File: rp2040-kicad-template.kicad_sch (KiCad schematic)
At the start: 48 parts, among them U1 RP2040, U2 TYPE-C-31-M-12, U3 XC6206PxxxMR, U4 PJ-320A, U5 USB Boot, U6 Reset, U7 W25Q16JVUXIQ, Y1 12MHz - 20pF

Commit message: Add parts libraries
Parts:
- removed D1: 5819W, Diode_SMD:D_SOD-123, symbol Device:D_Schottky_Small
- removed TP1: Debug 5V, TestPoint:TestPoint_Pad_D2.0mm, symbol Connector:TestPoint_Small
- removed U2: TYPE-C-31-M-12, footprints:simple-usb-c, symbol simple-usb-c:TYPE-C-31-M-12
- removed U4: PJ-320A, footprints:trrs-connector-pj320a, symbol trss-connector-pj320a:PJ-320A
- added U4: TYPE-C-31-M-12, footprint:USB-C_SMD-TYPE-C-31-M-12, symbol simple-usb-c:TYPE-C-31-M-12
- added U8: PJ-320A, footprint:AUDIO-TH_XKB_PJ-320A, symbol trrs-connector-pj320a:PJ-320A
- U3: footprint Package_TO_SOT_SMD:SOT-23 -> Package_TO_SOT_SMD:SOT-23-3
- U7: footprint footprints:w25q16jvuxiq -> footprint:USON-8_L3.0-W2.0-P0.50-BL-EP; LCSC Part # (none) -> C2843335
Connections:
- net CC1: now also U4.A5 (CC1)
- net CC2: now also U4.B5 (CC2)
- net GND: now also U4.A1 (GND), U4.A12 (GND), U4.B1 (GND), U4.B12 (GND), U8.5
- net SWCLK: now also U8.3
- net SWD: now also U8.4
- net USB+: now also U4.A6 (DP1), U4.B6 (DP2)
- net USB-: now also U4.A7 (DN1), U4.B7 (DN2)
- net VBUS: now also U4.A4 (VBUS), U4.A9 (VBUS), U4.B4 (VBUS), U4.B9 (VBUS)
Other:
- moved on the sheet: C11, C12, C13, C14, C15, C17, C18, C19, R7, R9, TP7, U3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

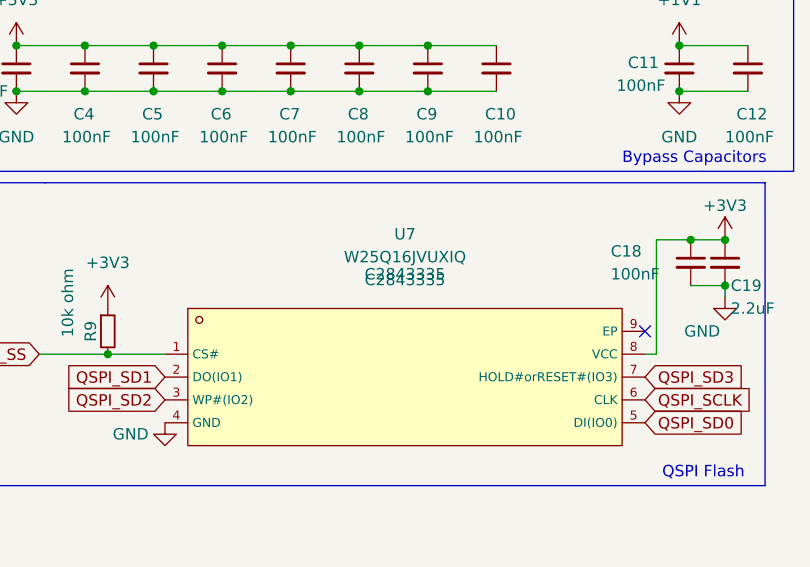
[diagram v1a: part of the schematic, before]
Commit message: Update some footprint references and use the newer footprint library
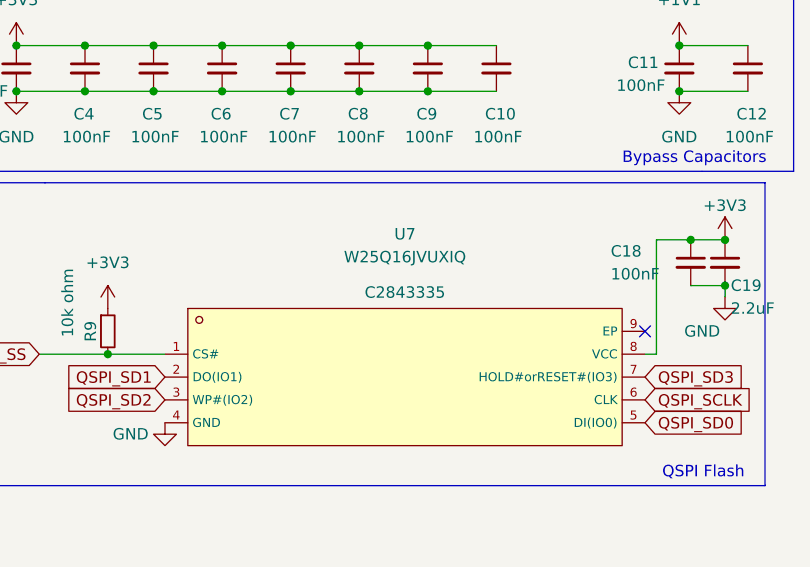
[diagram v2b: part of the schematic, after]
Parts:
- U4: footprint footprint:USB-C_SMD-TYPE-C-31-M-12 -> footprints:simple-usb-c
- U7: footprint footprint:USON-8_L3.0-W2.0-P0.50-BL-EP -> footprints:w25q16jvuxiq; LCSC Part # C2843335 -> (none)
- U8: footprint footprint:AUDIO-TH_XKB_PJ-320A -> footprints:trrs-connector-pj320a
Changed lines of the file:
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@@
 			)
 		)
-		(property "Footprint" "footprint:AUDIO-TH_XKB_PJ-320A"
+		(property "Footprint" "footprints:trrs-connector-pj320a"
 			(at 73.66 55.88 0)
 			(effects
@@
 		(on_board yes)
 		(dnp no)
-		(fields_autoplaced yes)
 		(property "Reference" "U7"
 			(at 240.03 42.545 0)
@@
 			)
 		)
-		(property "Footprint" "footprint:USON-8_L3.0-W2.0-P0.50-BL-EP"
+		(property "Footprint" "footprints:w25q16jvuxiq"
 			(at 240.03 57.15 0)
 			(effects
@@
 		)
 		(property "LCSC" "C2843335"
-			(at 240.03 47.625 0)
-			(effects
-				(font
-					(size 1.27 1.27)
-				)
-			)
-		)
-		(property "LCSC Part #" "C2843335"
-			(at 240.03 46.99 0)
+			(at 240.03 49.022 0)
 			(effects
 				(font
@@
 	)
 	(symbol
-		(lib_name "simple-usb-c:TYPE-C-31-M-12")
 		(lib_id "simple-usb-c:TYPE-C-31-M-12")
 		(at 34.29 25.4 0)
@@
 			)
 		)
-		(property "Footprint" "footprint:USB-C_SMD-TYPE-C-31-M-12"
+		(property "Footprint" "footprints:simple-usb-c"
 			(at 34.29 35.56 0)
 			(effects

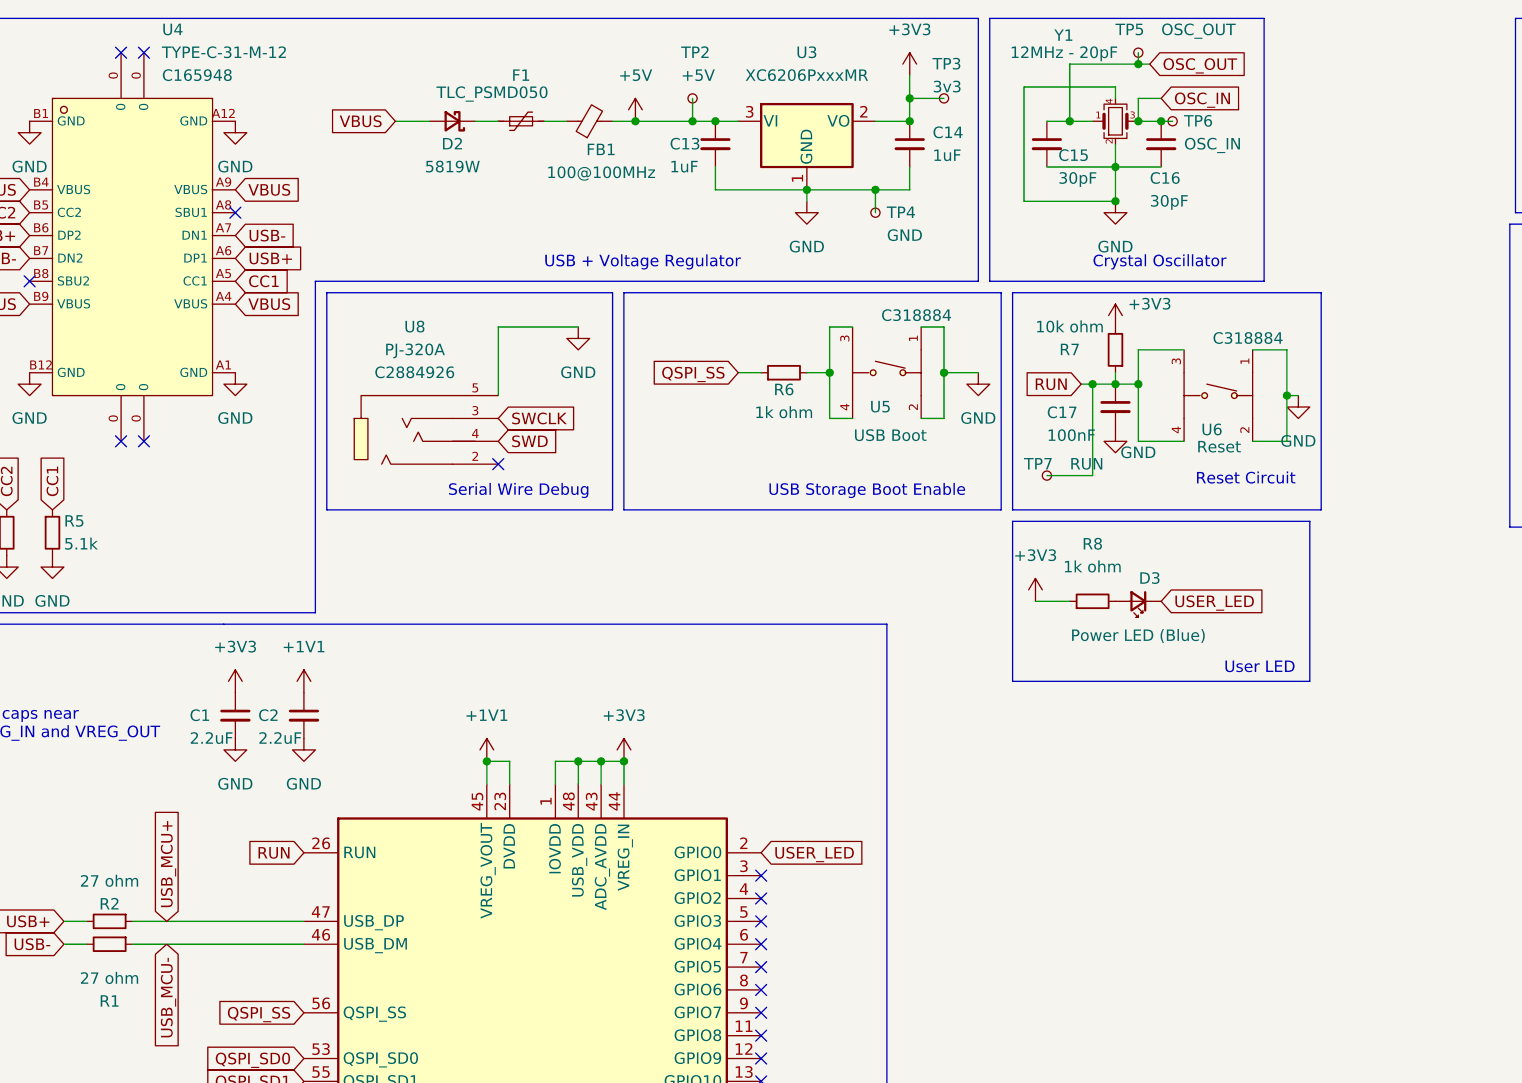
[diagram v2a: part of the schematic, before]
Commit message: Update the parts lib to include an ESD protection diode for USB 2.0
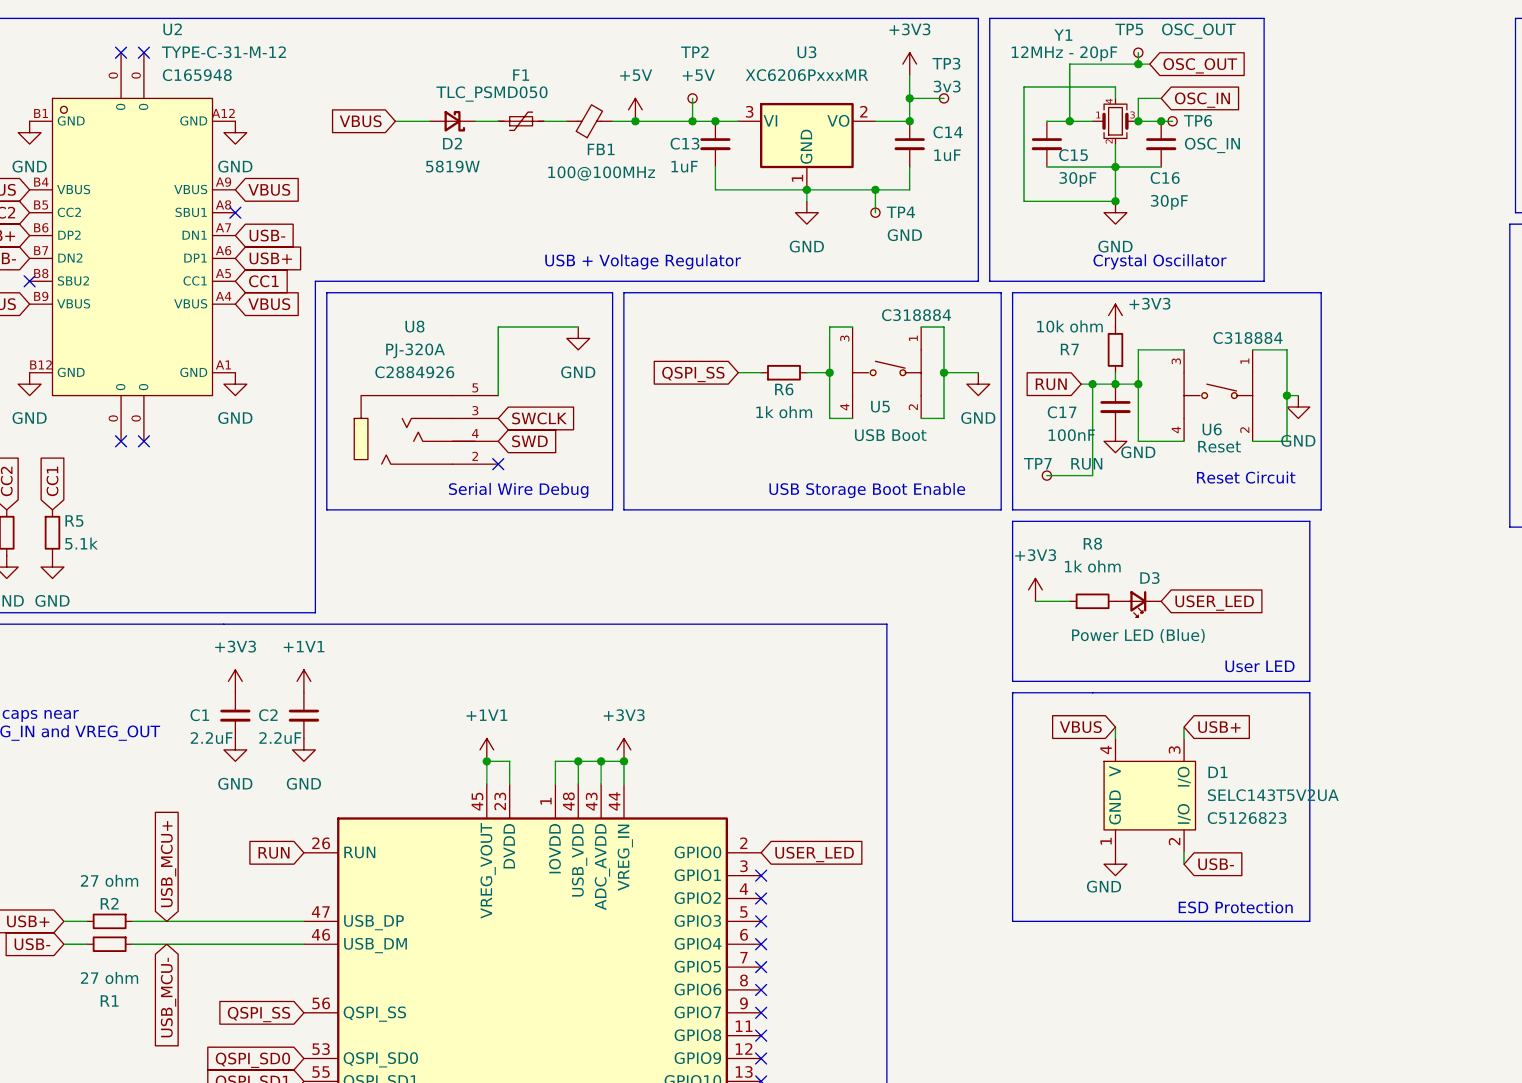
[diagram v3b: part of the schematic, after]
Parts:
- removed U4: TYPE-C-31-M-12, footprints:simple-usb-c, symbol simple-usb-c:TYPE-C-31-M-12
- added D1: SELC143T5V2UA, Package_TO_SOT_SMD:SOT-143, symbol usb_2_esd_protection:SELC143T5V2UA
- added U2: TYPE-C-31-M-12, footprints:simple-usb-c, symbol simple-usb-c:TYPE-C-31-M-12
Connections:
- net CC1: now also U2.A5 (CC1)
- net CC2: now also U2.B5 (CC2)
- net GND: now also D1.1 (GND), U2.A1 (GND), U2.A12 (GND), U2.B1 (GND), U2.B12 (GND)
- net USB+: now also D1.3 (I/O), U2.A6 (DP1), U2.B6 (DP2)
- net USB-: now also D1.2 (I/O), U2.A7 (DN1), U2.B7 (DN2)
- net VBUS: now also D1.4 (V), U2.A4 (VBUS), U2.A9 (VBUS), U2.B4 (VBUS), U2.B9 (VBUS)
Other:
- note added: "ESD Protection"
